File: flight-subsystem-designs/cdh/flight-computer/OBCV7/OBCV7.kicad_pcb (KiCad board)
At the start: 4 copper layers, 90.3 x 95.9 mm, 47 parts, among them U1 BEAGLEBONEBLACK, U3 TCAN337G, U4 MCP7940N-xSN, U6 MAX706RESA+T

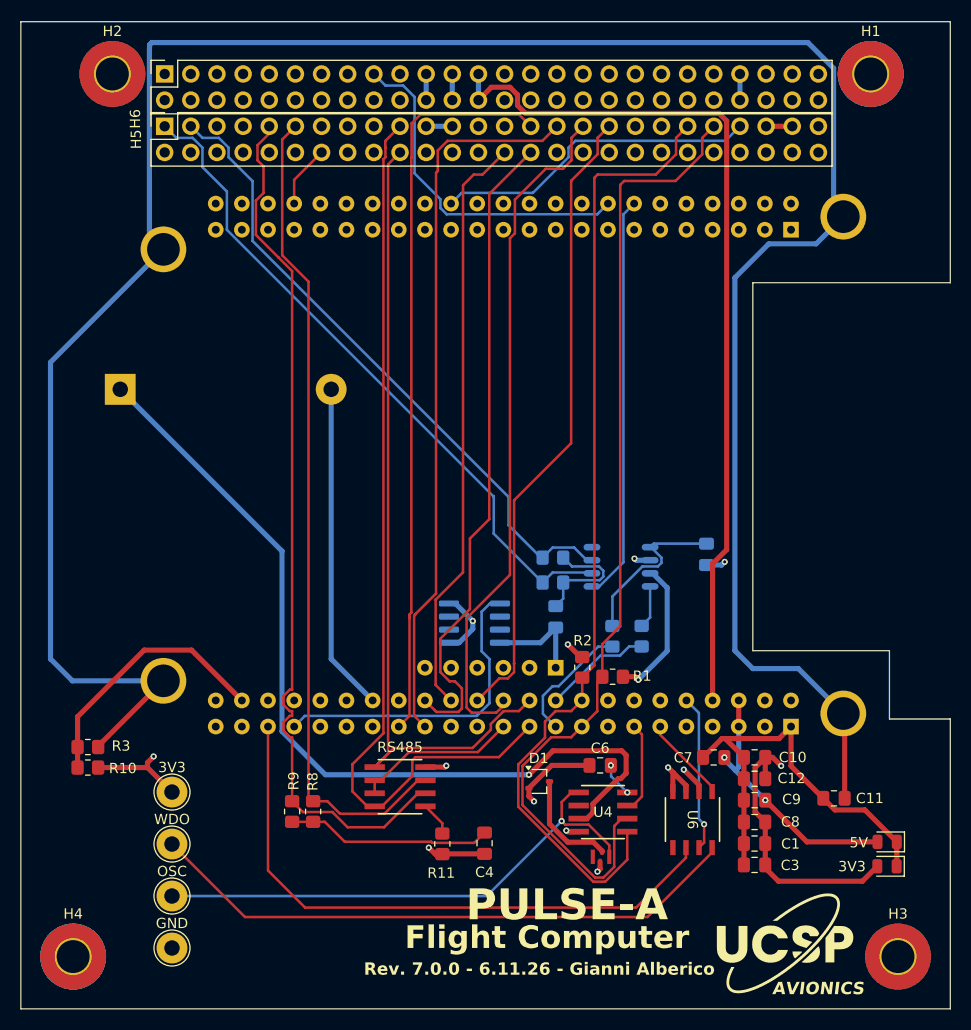
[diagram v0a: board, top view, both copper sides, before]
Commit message: perhaps technology is hubris manifest
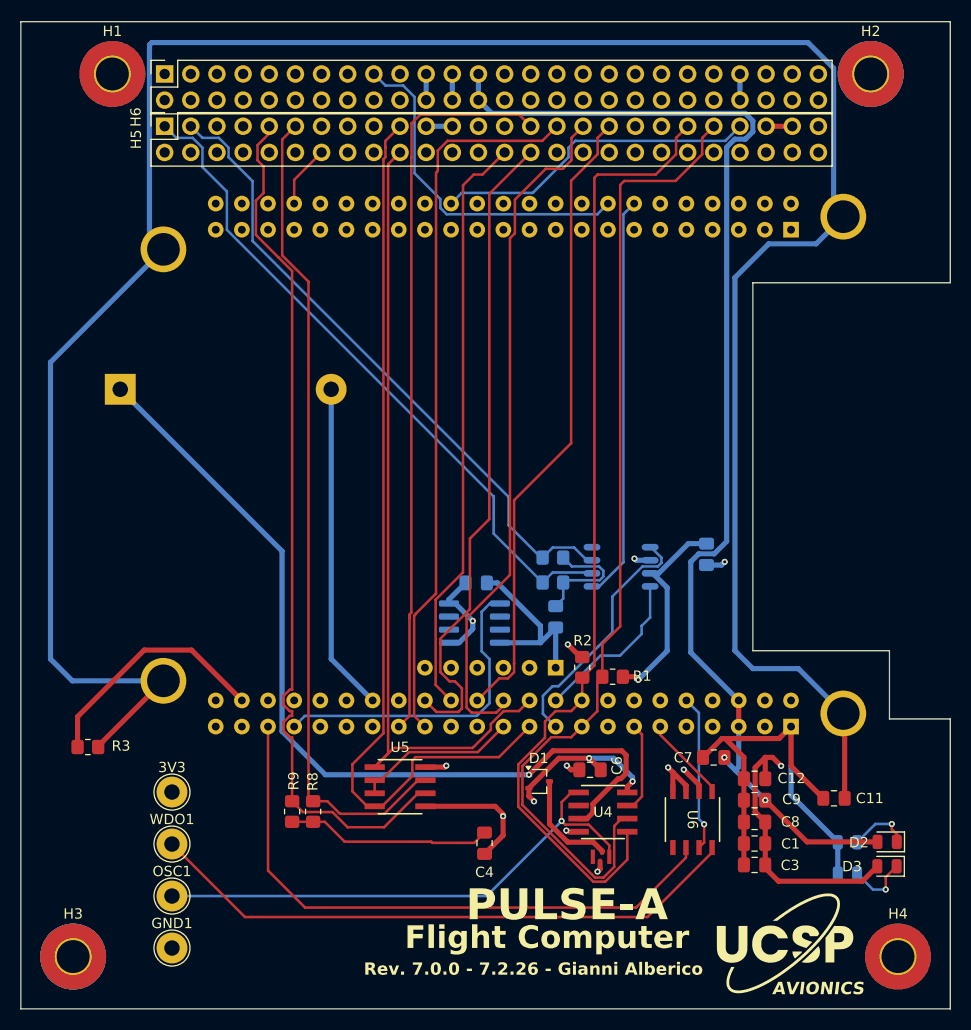
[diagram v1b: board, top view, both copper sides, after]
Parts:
- removed R10, R4, R5: 62, Resistor_SMD:R_0805_2012Metric_Pad1.20x1.40mm_HandSolder
- removed R11: 10k, Resistor_SMD:R_0805_2012Metric_Pad1.20x1.40mm_HandSolder
- added R12: 150, LED_SMD:LED_0805_2012Metric, B.Cu at (173.0, 110.1)
- added R13: 62, LED_SMD:LED_0805_2012Metric, B.Cu at (173.0, 113.2)
- 3V3: value TestPoint -> 3V3
- C10: moved to B.Cu
- OSC1: renamed from OSC; value CLKOUT -> OSC
- moved H3 80.1 mm to (97.8, 121.2)
- moved H4 80.1 mm to (177.9, 121.2)
- moved H1 73.7 mm to (101.6, 35.5)
- moved H2 73.7 mm to (175.2, 35.5)
- moved C10 31.9 mm to (136.9, 84.9), turned to 0 degrees
- moved C6 1.07 mm to (148.0, 103.1), turned to 180 degrees
- renumbered 5V to D2, 3V3 to D3, GND to GND1, RS485 to U5, TMP36XS to U7, WDO to WDO1
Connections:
- 3V3 pad 1: VDD_3V3B -> /3V3
- C1 pad 1: VDD_3V3B -> /3V3
- C10 pad 1: VDD_3V3B -> /3V3
- C12 pad 1: VDD_3V3B -> /3V3
- C2 pad 2: Net-(U3-TXD) -> /3V3
- C3 pad 1: VDD_3V3B -> /3V3
- C6 pad 1: VDD_3V3B -> /3V3
- C6 pad 2: Net-(U4-VCC) -> GND
- C8 pad 1: VDD_3V3B -> /3V3
- D1 pad 2: VDD_3V3B -> /3V3
- D2 pad 1: GND -> Net-(D2-K)
- D3 pad 1: GND -> Net-(D3-K)
- D3 pad 2: VDD_3V3B -> /3V3
- H5 pad 37: VDD_3V3B -> /3V3
- H6 pad 25: SYS_5V -> VDD_5V
- H6 pad 26: SYS_5V -> VDD_5V
- H6 pad 27: VDD_3V3B -> /3V3
- H6 pad 28: VDD_3V3B -> /3V3
- R1 pad 2: VDD_3V3B -> /3V3
- R2 pad 1: VDD_3V3B -> /3V3
- U1 pad P9_32: VDD_3V3B -> unconnected-(U1-VDD_ADC-PadP9_32)
- U1 pad P9_4: VDD_3V3B -> VDD_3V3B_1
- U3 pad 1: Net-(U3-TXD) -> /DCAN1TX
- U3 pad 3: VDD_3V3B -> /3V3
- U3 pad 4: Net-(U3-RXD) -> /DCAN1RX
- U4 pad 8: Net-(U4-VCC) -> /3V3
- U5 pad 5: Net-(U5-GND) -> GND
- U5 pad 8: VDD_3V3B -> /3V3
- U6 pad 2: VDD_3V3B -> /3V3
- U7 pad 5: VDD_3V3B -> /3V3
- U7 pad 8: VDD_3V3B -> /3V3
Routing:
- net VDD_5V: track 25.3 -> 117.5 mm
- net SYS_5V: track 86.0 -> 0.00 mm
- net /3V3: track 0.00 -> 81.1 mm, vias 0 -> 9
- net VDD_3V3B: track 72.7 -> 0.00 mm, vias 8 -> 0
- net GND: track 126.2 -> 145.9 mm, vias 6 -> 7
- net Net-(U3-TXD): track 16.6 -> 0.00 mm
- net /DCAN1TX: track 12.2 -> 24.4 mm
- net Net-(D2-K): track 0.00 -> 5.84 mm, vias 0 -> 1
- net Net-(D3-K): track 0.00 -> 5.60 mm, vias 0 -> 1
- net /DCAN1RX: track 10.5 -> 16.0 mm
- net Net-(U3-RXD): track 4.18 -> 0.00 mm
- net Net-(U5-GND): track 3.33 -> 0.00 mm
- net Net-(U4-VCC): track 3.29 -> 0.00 mm, vias 2 -> 0
- added copper zone on In2.Cu, net /3V3
- removed copper zone on In2.Cu, net VDD_3V3B
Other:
- board text added: "Rev. 7.0.0 - 7.2.26 - Gianni Alberico"
- board text added: "{dblquote}No, Im not playing on my phone, I'm taking care of business.{dblquote} -Eric Mays"
- board text removed: "Rev. 7.0.0 - 6.11.26 - Gianni Alberico"
- board text removed: "{dblquote}Im not playing on my phone, I'm taking care of business.{dblquote} -Eric Mays"

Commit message: Perhaps technology is hubris manifest
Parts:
- C3: moved to B.Cu
- C5: value 10nF -> 5nF
- moved C3 35.0 mm to (153.3, 79.0)
- turned U6 to 0 degrees
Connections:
- U1 pad P9_19: /DCAN1TX -> /DCAN0RX
- U1 pad P9_20: /DCAN1RX -> /DCAN0TX
- U3 pad 1: /DCAN1TX -> /DCAN0TX
- U3 pad 4: /DCAN1RX -> /DCAN0RX
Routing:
- net /DCAN1TX: track 24.4 -> 0.00 mm
- net /DCAN0TX: track 0.00 -> 19.4 mm
- net /DCAN0RX: track 0.00 -> 17.4 mm
- net /DCAN1RX: track 16.0 -> 0.00 mm
- net /3V3: track 81.1 -> 91.1 mm
- net Net-(U6-*WDO): track 58.5 -> 68.4 mm
- net /GPIO3_20: track 59.1 -> 62.7 mm
- net GND: track 145.9 -> 148.6 mm
- net /SYSRST: track 15.2 -> 12.5 mm
- net /MRV: track 8.39 -> 7.29 mm
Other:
- board text added: "Rev. 7.0.0 - 8.6.26 - Gianni Alberico"
- board text removed: "Rev. 7.0.0 - 7.2.26 - Gianni Alberico"

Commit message: Technology is truley hubris manifest
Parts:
- added R10: 10k, Resistor_SMD:R_0805_2012Metric_Pad1.20x1.40mm_HandSolder, B.Cu at (144.4, 79.8)
- added R4: 10k, Resistor_SMD:R_0805_2012Metric_Pad1.20x1.40mm_HandSolder, F.Cu at (156.1, 94.0)
- added R5: 10k, Resistor_SMD:R_0805_2012Metric_Pad1.20x1.40mm_HandSolder, F.Cu at (123.4, 102.8)
- C5: value 5nF -> 10nF
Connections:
- H6 pad 18: /ADCS_BOOT -> /ADCS_ENABLE
- H6 pad 20: /ADCS_ENABLE -> /ADCS_BOOT
- H6 pad 31: unconnected-(H6-Pin_31-Pad31) -> GND
- H6 pad 32: unconnected-(H6-Pin_32-Pad32) -> GND
- U3 pad 8: unconnected-(U3-S-Pad8) -> Net-(U3-S)
- U6 pad 8: Net-(U6-*WDO) -> /MRV
- WDO1 pad 1: Net-(U6-*WDO) -> /MRV
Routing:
- net /MRV: track 7.29 -> 83.4 mm
- net Net-(U6-*WDO): track 68.4 -> 0.00 mm
- net GND: track 148.6 -> 157.7 mm, vias 7 -> 8
- net /RTCC_MFP: track 8.90 -> 16.8 mm
- net /UART_TX: track 88.4 -> 93.5 mm
- net /GPIO1_17: track 15.9 -> 19.7 mm
- net Net-(U3-S): track 0.00 -> 3.40 mm
- net /3V3: track 91.1 -> 94.4 mm
